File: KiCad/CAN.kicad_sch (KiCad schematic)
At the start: 4 parts, among them U3 MCP2551-I-SN

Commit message: Modificació
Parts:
- renumbered J_CAN to J_CAN1
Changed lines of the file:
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@@
 		(dnp no)
 		(fields_autoplaced yes)
-		(property "Reference" "J_CAN"
+		(property "Reference" "J_CAN1"
 			(at 195.58 95.2499 0)
 			(effects
@@
 			(project ""
 				(path "/b6401b4f-5426-49b8-bb2e-8ecdb19989ef/0d9e3fa4-d4b2-4de6-93b6-04ac5a92c2ee"
-					(reference "J_CAN")
+					(reference "J_CAN1")
 					(unit 1)
 				)

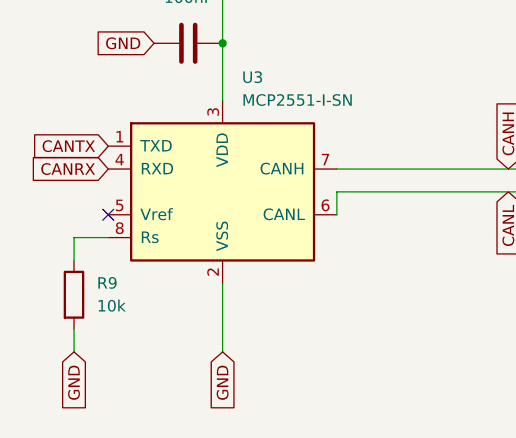
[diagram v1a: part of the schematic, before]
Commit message: Afegist el MOSFET
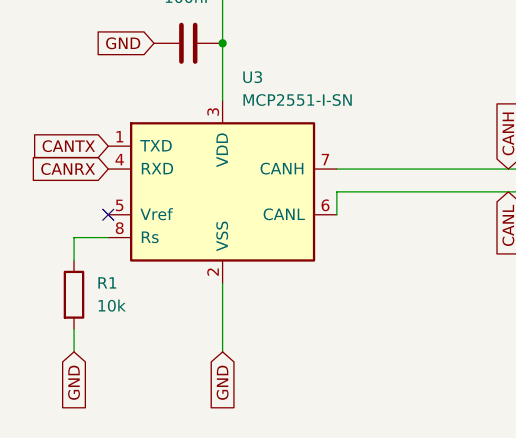
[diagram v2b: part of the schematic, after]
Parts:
- renumbered R9 to R1
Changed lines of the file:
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@@
+				)
+			)
+			(project "CAN"
+				(path "/ff967779-fbba-4a5a-a144-13183aa3df14"
+					(reference "C1")
+					(unit 1)
 				)
 			)
@@
 		(dnp no)
 		(fields_autoplaced yes)
-		(property "Reference" "J_CAN1"
+		(property "Reference" "J_CAN?"
 			(at 195.58 95.2499 0)
 			(effects
@@
 				(path "/b6401b4f-5426-49b8-bb2e-8ecdb19989ef/0d9e3fa4-d4b2-4de6-93b6-04ac5a92c2ee"
 					(reference "J_CAN1")
+					(unit 1)
+				)
+			)
+			(project "CAN"
+				(path "/ff967779-fbba-4a5a-a144-13183aa3df14"
+					(reference "J_CAN?")
 					(unit 1)
 				)
@@
 		(dnp no)
 		(fields_autoplaced yes)
-		(property "Reference" "R9"
+		(property "Reference" "R1"
 			(at 124.46 106.6799 0)
 			(effects
@@
 				(path "/b6401b4f-5426-49b8-bb2e-8ecdb19989ef/0d9e3fa4-d4b2-4de6-93b6-04ac5a92c2ee"
 					(reference "R9")
+					(unit 1)
+				)
+			)
+			(project "CAN"
+				(path "/ff967779-fbba-4a5a-a144-13183aa3df14"
+					(reference "R1")
 					(unit 1)
 				)
@@
 		(dnp no)
 		(fields_autoplaced yes)
-		(property "Reference" "U3"
+		(property "Reference" "U?"
 			(at 140.5733 83.82 0)
 			(effects
@@
 				)
 			)
-		)
-	)
+			(project "CAN"
+				(path "/ff967779-fbba-4a5a-a144-13183aa3df14"
+					(reference "U?")
+					(unit 1)
+				)
+			)
+		)
+	)
+	(sheet_instances
+		(path "/"
+			(page "1")
+		)
+	)
+	(embedded_fonts no)
 )

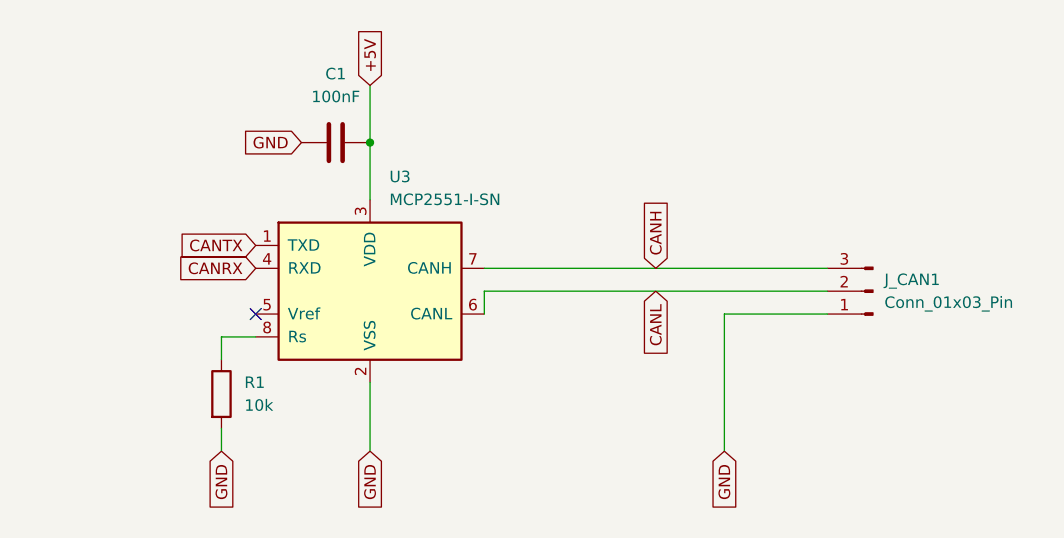
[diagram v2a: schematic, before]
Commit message: cambios mejora ERC
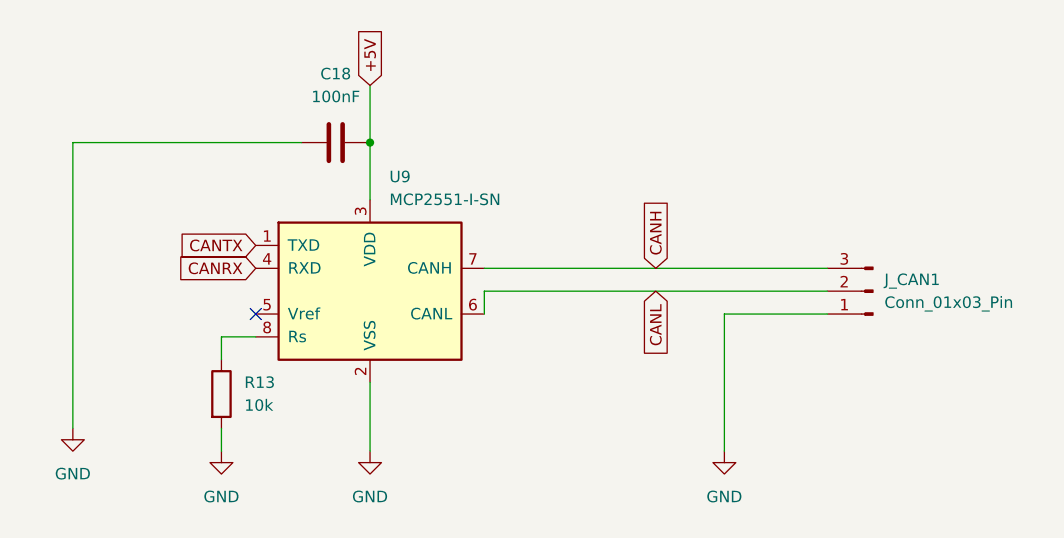
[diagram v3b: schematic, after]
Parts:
- renumbered C1 to C18, R1 to R13, U3 to U9

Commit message: ArregLATS ERRORS ERC
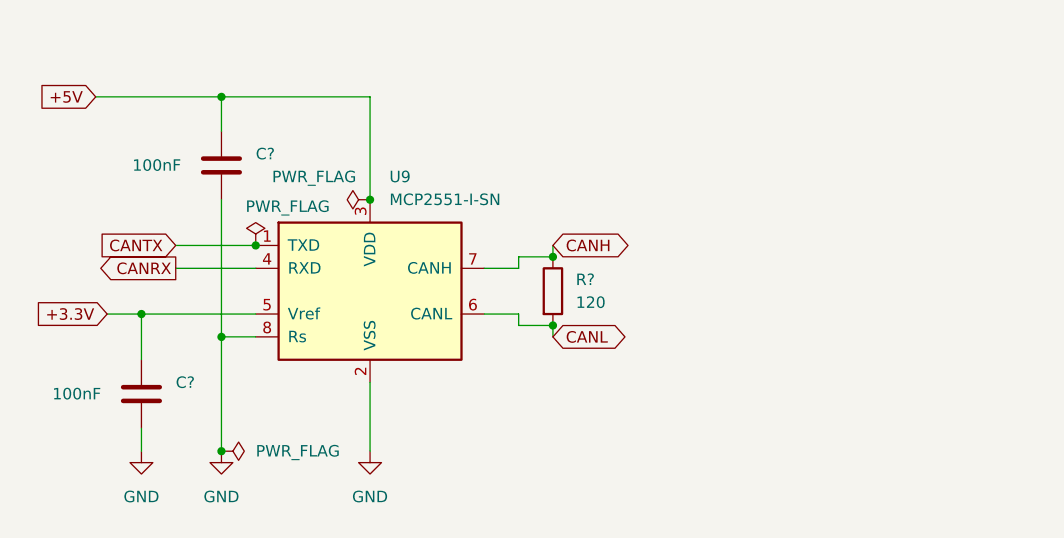
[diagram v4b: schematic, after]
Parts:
- removed J_CAN1: Conn_01x03_Pin, symbol Connector:Conn_01x03_Pin
- removed R13: 10k, symbol Device:R
- added C?: 100nF, symbol Device:C
- added R?: 120, symbol Device:R
- renumbered C18 to C?
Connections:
- net CANH: now also R?.1
- net CANL: now also R?.2
- net GND: now also U9.8 (Rs), C?.1
- net +3.3V: now reaches U9.5 (Vref)
- net +3.3V: now also C?.2
- no-connect marks 1 -> 0
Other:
- moved on the sheet: C?

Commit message: Modificacions Micro
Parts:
- gave numbers to parts that had none: 3
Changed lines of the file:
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@@
-	)
-	(junction
-		(at 121.92 114.3)
-		(diameter 0)
-		(color 0 0 0 0)
 	)
 	(junction
@@
 		)
 		(property "Intersheetrefs" "${INTERSHEET_REFS}"
-			(at 100.55 99.06 0)
+			(at 101.2042 99.06 0)
 			(effects
 				(font
@@
 		(on_board yes)
 		(dnp no)
-		(property "Reference" "C?"
+		(property "Reference" "C28"
 			(at 116.84 106.6799 0)
 			(effects
@@
 			(project "SEIENTS_EDD"
 				(path "/b6401b4f-5426-49b8-bb2e-8ecdb19989ef/0d9e3fa4-d4b2-4de6-93b6-04ac5a92c2ee"
-					(reference "C?")
+					(reference "C28")
 					(unit 1)
 				)
@@
 		(on_board yes)
 		(dnp no)
-		(property "Reference" "C?"
+		(property "Reference" "C29"
 			(at 125.73 81.2799 0)
 			(effects
@@
 			(project "SEIENTS_EDD"
 				(path "/b6401b4f-5426-49b8-bb2e-8ecdb19989ef/0d9e3fa4-d4b2-4de6-93b6-04ac5a92c2ee"
-					(reference "C?")
+					(reference "C29")
 					(unit 1)
 				)
@@
 	(symbol
 		(lib_id "power:PWR_FLAG")
-		(at 121.92 114.3 270)
-		(unit 1)
-		(exclude_from_sim no)
-		(in_bom yes)
-		(on_board yes)
-		(dnp no)
-		(fields_autoplaced yes)
-		(property "Reference" "#FLG?"
-			(at 123.825 114.3 0)
-			(effects
-				(font
-					(size 1.27 1.27)
-				)
-				(hide yes)
-			)
-		)
-		(property "Value" "PWR_FLAG"
-			(at 125.73 114.2999 90)
-			(effects
-				(font
-					(size 1.27 1.27)
-				)
-				(justify left)
-			)
-		)
-		(property "Footprint" ""
-			(at 121.92 114.3 0)
-			(effects
-				(font
-					(size 1.27 1.27)
-				)
-				(hide yes)
-			)
-		)
-		(property "Datasheet" "~"
-			(at 121.92 114.3 0)
-			(effects
-				(font
-					(size 1.27 1.27)
-				)
-				(hide yes)
-			)
-		)
-		(property "Description" "Special symbol for telling ERC where power comes from"
-			(at 121.92 114.3 0)
-			(effects
-				(font
-					(size 1.27 1.27)
-				)
-				(hide yes)
-			)
-		)
-		(pin "1"
-		)
-		(instances
-			(project "SEIENTS_EDD"
-				(path "/b6401b4f-5426-49b8-bb2e-8ecdb19989ef/0d9e3fa4-d4b2-4de6-93b6-04ac5a92c2ee"
-					(reference "#FLG?")
-					(unit 1)
-				)
-			)
-			(project ""
-				(path "/ff967779-fbba-4a5a-a144-13183aa3df14"
-					(reference "#FLG01")
-					(unit 1)
-				)
-			)
-		)
-	)
-	(symbol
-		(lib_id "power:PWR_FLAG")
 		(at 125.73 91.44 0)
 		(unit 1)
@@
 		(on_board yes)
 		(dnp no)
-		(property "Reference" "#FLG?"
+		(property "Reference" "#FLG013"
 			(at 125.73 89.535 0)
 			(effects
@@
 			(project "SEIENTS_EDD"
 				(path "/b6401b4f-5426-49b8-bb2e-8ecdb19989ef/0d9e3fa4-d4b2-4de6-93b6-04ac5a92c2ee"
-					(reference "#FLG?")
+					(reference "#FLG013")
 					(unit 1)
 				)
@@
 		(dnp no)
 		(fields_autoplaced yes)
-		(property "Reference" "R?"
+		(property "Reference" "R21"
 			(at 161.29 95.2499 0)
 			(effects
@@
 			(project "SEIENTS_EDD"
 				(path "/b6401b4f-5426-49b8-bb2e-8ecdb19989ef/0d9e3fa4-d4b2-4de6-93b6-04ac5a92c2ee"
-					(reference "R?")
+					(reference "R21")
 					(unit 1)
 				)
@@
 		(on_board yes)
 		(dnp no)
-		(property "Reference" "#FLG?"
+		(property "Reference" "#FLG014"
 			(at 136.525 86.36 0)
 			(effects
@@
 			(project "SEIENTS_EDD"
 				(path "/b6401b4f-5426-49b8-bb2e-8ecdb19989ef/0d9e3fa4-d4b2-4de6-93b6-04ac5a92c2ee"
-					(reference "#FLG?")
-					(unit 1)
-				)
+					(reference "#FLG014")
+					(unit 1)
+				)

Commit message: Començat el LAYOUT
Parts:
- removed U9: MCP2551-I-SN, Package_SO:SOIC-8_3.9x4.9mm_P1.27mm, symbol Interface_CAN_LIN:MCP2551-I-SN
- added U13: MCP2562-E-SN, Package_SO:SOIC-8_3.9x4.9mm_P1.27mm, symbol Interface_CAN_LIN:MCP2562-E-SN
- R21: footprint (none) -> Resistor_SMD:R_0805_2012Metric
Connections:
- net +3.3V: now also U13.5 (Vio)
- net +5V: now also U13.3 (VDD)
- net CANH: now also U13.7 (CANH)
- net CANL: now also U13.6 (CANL)
- net CANRX: now also U13.4 (RXD)
- net CANTX: now also U13.1 (TXD)
- net GND: now also U13.2 (VSS), U13.8 (STBY)
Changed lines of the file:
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@@
 	(paper "A4")
 	(junction
-		(at 125.73 91.44)
+		(at 138.43 86.36)
 		(diameter 0)
 		(color 0 0 0 0)
@@
 	(junction
 		(at 158.75 100.33)
-		(diameter 0)
-		(color 0 0 0 0)
-	)
-	(junction
-		(at 138.43 86.36)
 		(diameter 0)
 		(color 0 0 0 0)
@@
 	)
 	(symbol
+		(lib_id "Interface_CAN_LIN:MCP2562-E-SN")
+		(at 138.43 96.52 0)
+		(unit 1)
+		(exclude_from_sim no)
+		(in_bom yes)
+		(on_board yes)
+		(dnp no)
+		(fields_autoplaced yes)
+		(property "Reference" "U13"
+			(at 140.5733 83.82 0)
+			(effects
+				(font
+					(size 1.27 1.27)
+				)
+				(justify left)
+			)
+		)
+		(property "Value" "MCP2562-E-SN"
+			(at 140.5733 86.36 0)
+			(effects
+				(font
+					(size 1.27 1.27)
+				)
+				(justify left)
+			)
+		)
+		(property "Footprint" "Package_SO:SOIC-8_3.9x4.9mm_P1.27mm"
+			(at 138.43 109.22 0)
+			(effects
+				(font
+					(size 1.27 1.27)
+					(italic yes)
+				)
+				(hide yes)
+			)
+		)
+		(property "Datasheet" "http://ww1.microchip.com/downloads/en/DeviceDoc/25167A.pdf"
+			(at 138.43 96.52 0)
+			(effects
+				(font
+					(size 1.27 1.27)
+				)
+				(hide yes)
+			)
+		)
+		(property "Description" "High-Speed CAN Transceiver, 1Mbps, 5V supply, Vio pin, -40C to +125C, SOIC-8"
+			(at 138.43 96.52 0)
+			(effects
+				(font
+					(size 1.27 1.27)
+				)
+				(hide yes)
+			)
+		)
+		(pin "6"
+		)
+		(pin "8"
+		)
+		(pin "7"
+		)
+		(pin "3"
+		)
+		(pin "5"
+		)
+		(pin "2"
+		)
+		(pin "1"
+		)
+		(pin "4"
+		)
+		(instances
+			(project ""
+				(path "/b6401b4f-5426-49b8-bb2e-8ecdb19989ef/0d9e3fa4-d4b2-4de6-93b6-04ac5a92c2ee"
+					(reference "U13")
+					(unit 1)
+				)
+			)
+		)
+	)
+	(symbol
 		(lib_id "power:GND")
 		(at 138.43 114.3 0)
@@
 				(path "/ff967779-fbba-4a5a-a144-13183aa3df14"
 					(reference "#PWR02")
-					(unit 1)
-				)
-			)
-		)
-	)
-	(symbol
-		(lib_id "power:PWR_FLAG")
-		(at 125.73 91.44 0)
-		(unit 1)
-		(exclude_from_sim no)
-		(in_bom yes)
-		(on_board yes)
-		(dnp no)
-		(property "Reference" "#FLG013"
-			(at 125.73 89.535 0)
-			(effects
-				(font
-					(size 1.27 1.27)
-				)
-				(hide yes)
-			)
-		)
-		(property "Value" "PWR_FLAG"
-			(at 129.286 87.122 0)
-			(effects
-				(font
-					(size 1.27 1.27)
-				)
-			)
-		)
-		(property "Footprint" ""
-			(at 125.73 91.44 0)
-			(effects
-				(font
-					(size 1.27 1.27)
-				)
-				(hide yes)
-			)
-		)
-		(property "Datasheet" "~"
-			(at 125.73 91.44 0)
-			(effects
-				(font
-					(size 1.27 1.27)
-				)
-				(hide yes)
-			)
-		)
-		(property "Description" "Special symbol for telling ERC where power comes from"
-			(at 125.73 91.44 0)
-			(effects
-				(font
-					(size 1.27 1.27)
-				)
-				(hide yes)
-			)
-		)
-		(pin "1"
-		)
-		(instances
-			(project "SEIENTS_EDD"
-				(path "/b6401b4f-5426-49b8-bb2e-8ecdb19989ef/0d9e3fa4-d4b2-4de6-93b6-04ac5a92c2ee"
-					(reference "#FLG013")
-					(unit 1)
-				)
-			)
-			(project "CAN"
-				(path "/ff967779-fbba-4a5a-a144-13183aa3df14"
-					(reference "#FLG03")
 					(unit 1)
 				)
@@
 			)
 		)
-		(property "Footprint" ""
+		(property "Footprint" "Resistor_SMD:R_0805_2012Metric"
 			(at 156.972 96.52 90)
 			(effects
@@
 					(unit 1)
 				)
-			)
-		)
-	)
-	(symbol
-		(lib_id "Interface_CAN_LIN:MCP2551-I-SN")
-		(at 138.43 96.52 0)
-		(unit 1)
-		(exclude_from_sim no)
-		(in_bom yes)
-		(on_board yes)
-		(dnp no)
-		(fields_autoplaced yes)
-		(property "Reference" "U9"
-			(at 140.5733 83.82 0)
-			(effects
-				(font
-					(size 1.27 1.27)
-				)
-				(justify left)
-			)
-		)
-		(property "Value" "MCP2551-I-SN"
-			(at 140.5733 86.36 0)
-			(effects
-				(font
-					(size 1.27 1.27)
-				)
-				(justify left)
-			)
-		)
-		(property "Footprint" "Package_SO:SOIC-8_3.9x4.9mm_P1.27mm"
-			(at 138.43 109.22 0)
-			(effects
-				(font
-					(size 1.27 1.27)
-					(italic yes)
-				)
-				(hide yes)
-			)
-		)
-		(property "Datasheet" "http://ww1.microchip.com/downloads/en/devicedoc/21667d.pdf"
-			(at 138.43 96.52 0)
-			(effects
-				(font
-					(size 1.27 1.27)
-				)
-				(hide yes)
-			)
-		)
-		(property "Description" "High-Speed CAN Transceiver, 1Mbps, 5V supply, SOIC-8"
-			(at 138.43 96.52 0)
-			(effects
-				(font
-					(size 1.27 1.27)
-				)
-				(hide yes)
-			)
-		)
-		(pin "1"
-		)
-		(pin "4"
-		)
-		(pin "8"
-		)
-		(pin "3"
-		)
-		(pin "6"
-		)
-		(pin "5"
-		)
-		(pin "2"
-		)
-		(pin "7"
-		)
-		(instances
-			(project ""
-				(path "/b6401b4f-5426-49b8-bb2e-8ecdb19989ef/0d9e3fa4-d4b2-4de6-93b6-04ac5a92c2ee"
-					(reference "U9")
-					(unit 1)
-				)
-			)
-			(project "CAN"
-				(path "/ff967779-fbba-4a5a-a144-13183aa3df14"
-					(reference "U13")
-					(unit 1)
-				)

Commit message: footprints asignados
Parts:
- C28, C29: footprint (none) -> Capacitor_SMD:C_0805_2012Metric
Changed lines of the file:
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@@
 			)
 		)
-		(property "Footprint" ""
+		(property "Footprint" "Capacitor_SMD:C_0805_2012Metric"
 			(at 112.0648 104.14 0)
 			(effects
@@
 			)
 		)
-		(property "Footprint" ""
+		(property "Footprint" "Capacitor_SMD:C_0805_2012Metric"
 			(at 120.9548 78.74 0)
 			(effects
